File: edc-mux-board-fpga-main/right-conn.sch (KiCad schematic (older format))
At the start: 68 parts, among them J10 Device 7, J7 Device 4, J8 Device 5, J9 Device 6

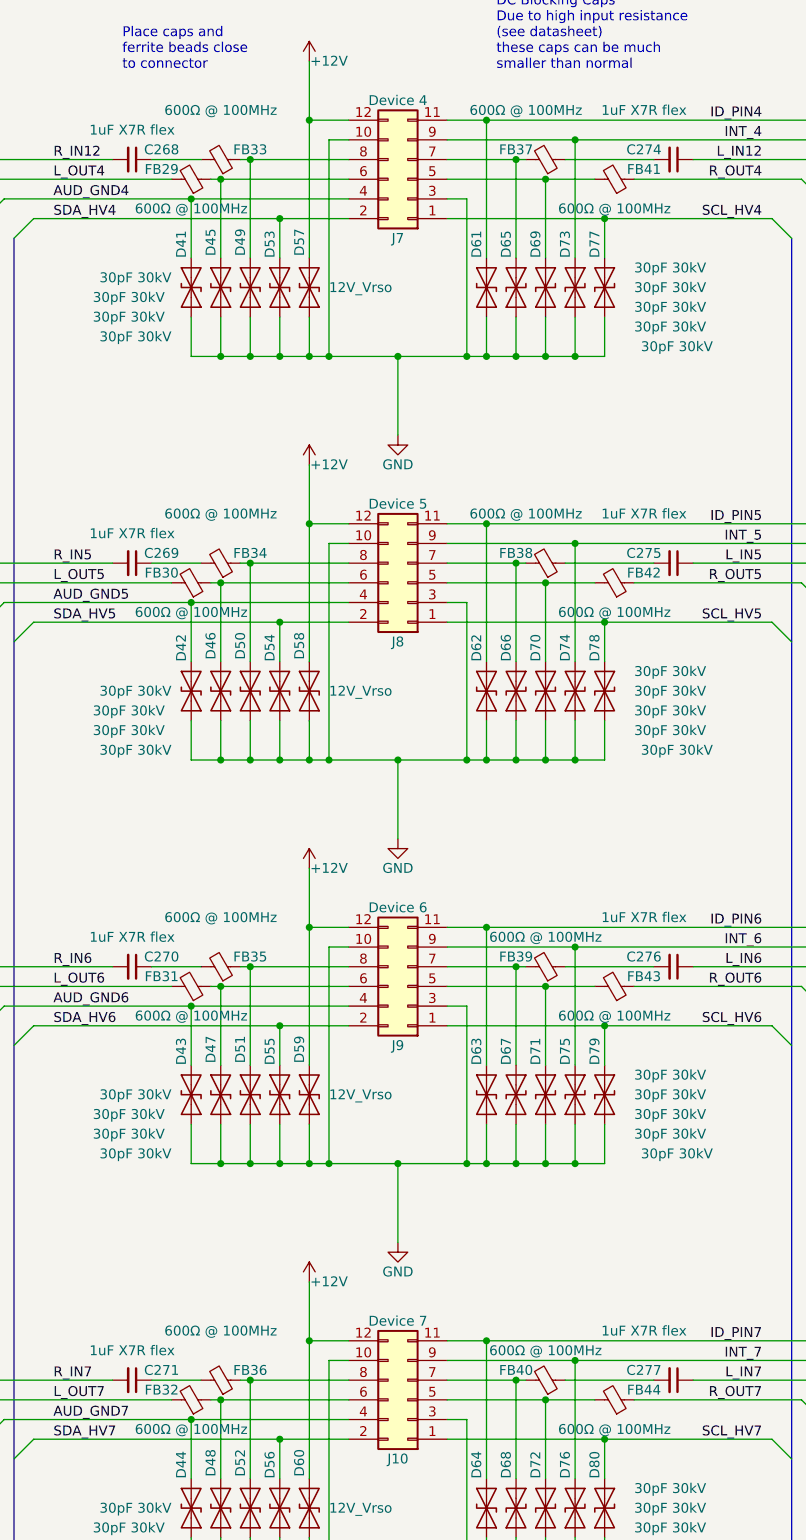
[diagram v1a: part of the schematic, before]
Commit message: Reannotate main schematic and pcb after expansion transition
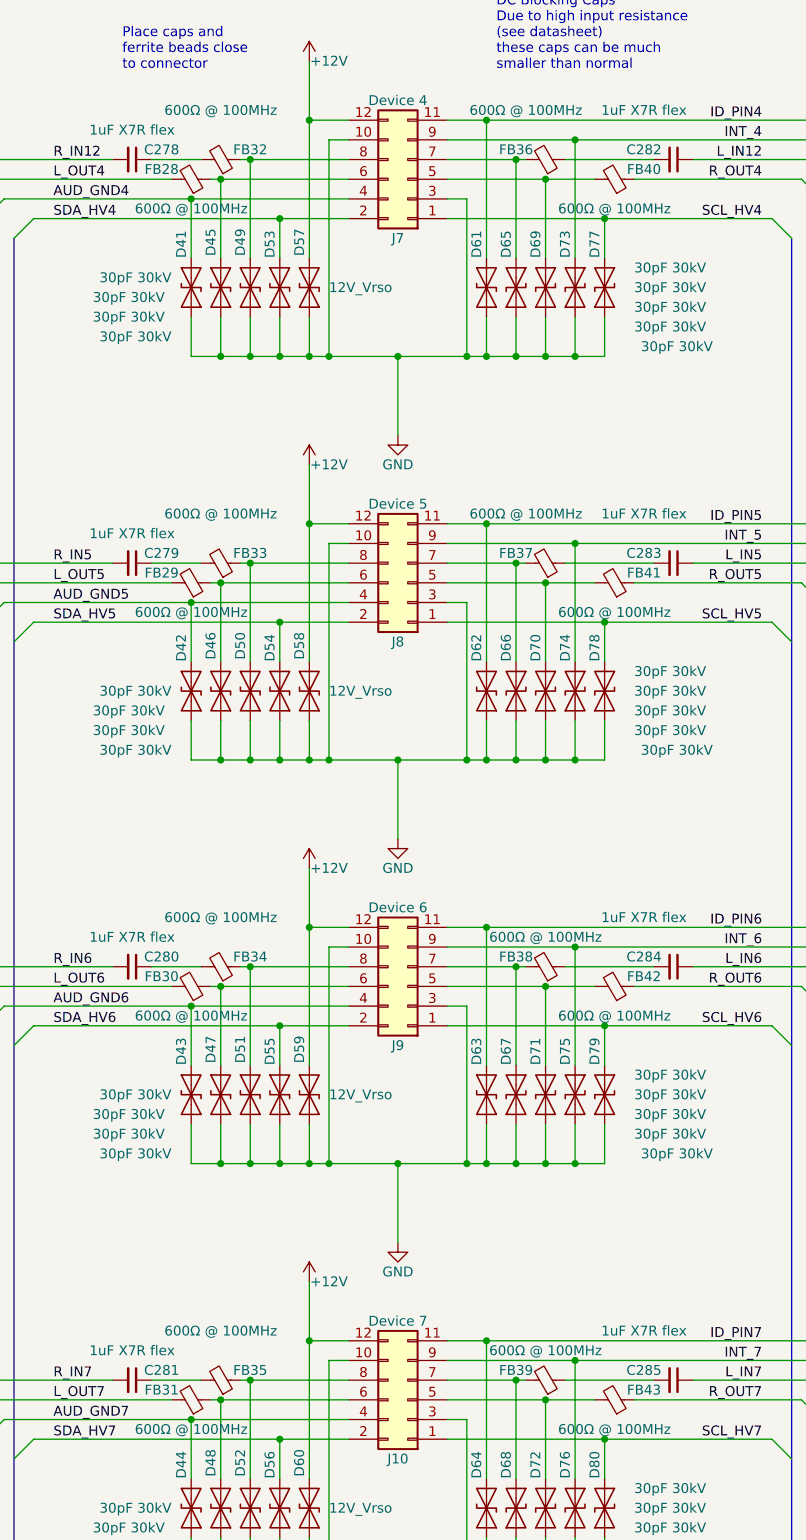
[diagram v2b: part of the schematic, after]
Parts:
- renumbered C268 to C278, C269 to C279, C270 to C280, C271 to C281, C274 to C282, C275 to C283, C276 to C284, C277 to C285, FB29 to FB28, FB30 to FB29, FB31 to FB30, FB32 to FB31, FB33 to FB32, FB34 to FB33, FB35 to FB34, FB36 to FB35, FB37 to FB36, FB38 to FB37, FB39 to FB38, FB40 to FB39, FB41 to FB40, FB42 to FB41, FB43 to FB42, FB44 to FB43
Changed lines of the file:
@@
 	4900 3100 5000 3100
 $Comp
-L power:GND #PWR0121
+L power:GND #PWR0133
 U 1 1 5D2BDD3D
 P 4550 3500
-F 0 "#PWR0121" H 4550 3250 50  0001 C CNN
+F 0 "#PWR0133" H 4550 3250 50  0001 C CNN
 F 1 "GND" H 4550 3350 50  0000 C CNN
 F 2 "" H 4550 3500 50  0001 C CNN
@@
 INT_4
 $Comp
-L power:+12V #PWR0117
+L power:+12V #PWR0129
 U 1 1 5D2BDD51
 P 4100 1600
-F 0 "#PWR0117" H 4100 1450 50  0001 C CNN
+F 0 "#PWR0129" H 4100 1450 50  0001 C CNN
 F 1 "+12V" H 4200 1600 50  0000 C CNN
 F 2 "" H 4100 1600 50  0001 C CNN
@@
 	4800 2400 5600 2400
 $Comp
-L Device:Ferrite_Bead_Small FB37
+L Device:Ferrite_Bead_Small FB36
 U 1 1 5D2BDD5F
 P 5300 2100
-F 0 "FB37" V 5350 1950 50  0000 C CNN
+F 0 "FB36" V 5350 1950 50  0000 C CNN
 F 1 "600Ω @ 100MHz" V 5550 2000 50  0000 C CNN
 F 2 "Inductor_SMD:L_0805_2012Metric" V 5230 2100 50  0001 C CNN
@@
 	3600 2200 3650 2200
 $Comp
-L Device:C_Small C268
+L Device:C_Small C278
 U 1 1 5D2BDD6B
 P 3200 2100
-F 0 "C268" V 3150 2250 50  0000 C CNN
+F 0 "C278" V 3150 2250 50  0000 C CNN
 F 1 "1uF X7R flex" V 3050 2100 50  0000 C CNN
 F 2 "Capacitor_SMD:C_0805_2012Metric" H 3200 2100 50  0001 C CNN
@@
 $EndComp
 $Comp
-L Device:Ferrite_Bead_Small FB33
+L Device:Ferrite_Bead_Small FB32
 U 1 1 5D2BDD77
 P 3650 2100
-F 0 "FB33" V 3700 2250 50  0000 C CNN
+F 0 "FB32" V 3700 2250 50  0000 C CNN
 F 1 "600Ω @ 100MHz" V 3900 2100 50  0000 C CNN
 F 2 "Inductor_SMD:L_0805_2012Metric" V 3580 2100 50  0001 C CNN
@@
 $EndComp
 $Comp
-L Device:Ferrite_Bead_Small FB29
+L Device:Ferrite_Bead_Small FB28
 U 1 1 5D2BDD82
 P 3500 2200
-F 0 "FB29" V 3550 2050 50  0000 C CNN
+F 0 "FB28" V 3550 2050 50  0000 C CNN
 F 1 "600Ω @ 100MHz" V 3350 2200 50  0000 C CNN
 F 2 "Inductor_SMD:L_0805_2012Metric" V 3430 2200 50  0001 C CNN
@@
 $EndComp
 $Comp
-L Device:Ferrite_Bead_Small FB41
+L Device:Ferrite_Bead_Small FB40
 U 1 1 5D2BDD8D
 P 5650 2200
-F 0 "FB41" V 5700 2350 50  0000 C CNN
+F 0 "FB40" V 5700 2350 50  0000 C CNN
 F 1 "600Ω @ 100MHz" V 5500 2200 50  0000 C CNN
 F 2 "Inductor_SMD:L_0805_2012Metric" V 5580 2200 50  0001 C CNN
@@
 $EndComp
 $Comp
-L Device:C_Small C274
+L Device:C_Small C282
 U 1 1 5D2BDD99
 P 5950 2100
-F 0 "C274" V 5900 1950 50  0000 C CNN
+F 0 "C282" V 5900 1950 50  0000 C CNN
 F 1 "1uF X7R flex" V 5700 1950 50  0000 C CNN
 F 2 "Capacitor_SMD:C_0805_2012Metric" H 5950 2100 50  0001 C CNN
@@
 	4900 5150 5000 5150
 $Comp
-L power:GND #PWR0122
+L power:GND #PWR0134
 U 1 1 5D2BDE54
 P 4550 5550
-F 0 "#PWR0122" H 4550 5300 50  0001 C CNN
+F 0 "#PWR0134" H 4550 5300 50  0001 C CNN
 F 1 "GND" H 4550 5400 50  0000 C CNN
 F 2 "" H 4550 5550 50  0001 C CNN
@@
 INT_5
 $Comp
-L power:+12V #PWR0118
+L power:+12V #PWR0130
 U 1 1 5D2BDE68
 P 4100 3650
-F 0 "#PWR0118" H 4100 3500 50  0001 C CNN
+F 0 "#PWR0130" H 4100 3500 50  0001 C CNN
 F 1 "+12V" H 4200 3650 50  0000 C CNN
 F 2 "" H 4100 3650 50  0001 C CNN
@@
 	4800 4450 5600 4450
 $Comp
-L Device:Ferrite_Bead_Small FB38
+L Device:Ferrite_Bead_Small FB37
 U 1 1 5D2BDE76
 P 5300 4150
-F 0 "FB38" V 5350 4000 50  0000 C CNN
+F 0 "FB37" V 5350 4000 50  0000 C CNN
 F 1 "600Ω @ 100MHz" V 5550 4050 50  0000 C CNN
 F 2 "Inductor_SMD:L_0805_2012Metric" V 5230 4150 50  0001 C CNN
@@
 	3600 4250 3650 4250
 $Comp
-L Device:C_Small C269
+L Device:C_Small C279
 U 1 1 5D2BDE82
 P 3200 4150
-F 0 "C269" V 3150 4300 50  0000 C CNN
+F 0 "C279" V 3150 4300 50  0000 C CNN
 F 1 "1uF X7R flex" V 3050 4150 50  0000 C CNN
 F 2 "Capacitor_SMD:C_0805_2012Metric" H 3200 4150 50  0001 C CNN
@@
 $EndComp
 $Comp
-L Device:Ferrite_Bead_Small FB34
+L Device:Ferrite_Bead_Small FB33
 U 1 1 5D2BDE8E
 P 3650 4150
-F 0 "FB34" V 3700 4300 50  0000 C CNN
+F 0 "FB33" V 3700 4300 50  0000 C CNN
 F 1 "600Ω @ 100MHz" V 3900 4150 50  0000 C CNN
 F 2 "Inductor_SMD:L_0805_2012Metric" V 3580 4150 50  0001 C CNN
@@
 $EndComp
 $Comp
-L Device:Ferrite_Bead_Small FB30
+L Device:Ferrite_Bead_Small FB29
 U 1 1 5D2BDE99
 P 3500 4250
-F 0 "FB30" V 3550 4100 50  0000 C CNN
+F 0 "FB29" V 3550 4100 50  0000 C CNN
 F 1 "600Ω @ 100MHz" V 3350 4250 50  0000 C CNN
 F 2 "Inductor_SMD:L_0805_2012Metric" V 3430 4250 50  0001 C CNN
@@
 $EndComp
 $Comp
-L Device:Ferrite_Bead_Small FB42
+L Device:Ferrite_Bead_Small FB41
 U 1 1 5D2BDEA4
 P 5650 4250
-F 0 "FB42" V 5700 4400 50  0000 C CNN
+F 0 "FB41" V 5700 4400 50  0000 C CNN
 F 1 "600Ω @ 100MHz" V 5500 4250 50  0000 C CNN
 F 2 "Inductor_SMD:L_0805_2012Metric" V 5580 4250 50  0001 C CNN
@@
 $EndComp
 $Comp
-L Device:C_Small C275
+L Device:C_Small C283
 U 1 1 5D2BDEB0
 P 5950 4150
-F 0 "C275" V 5900 4000 50  0000 C CNN
+F 0 "C283" V 5900 4000 50  0000 C CNN
 F 1 "1uF X7R flex" V 5700 4000 50  0000 C CNN
 F 2 "Capacitor_SMD:C_0805_2012Metric" H 5950 4150 50  0001 C CNN
@@
 	4900 7200 5000 7200
 $Comp
-L power:GND #PWR0123
+L power:GND #PWR0135
 U 1 1 5D2BDF6B
 P 4550 7600
-F 0 "#PWR0123" H 4100 7950 50  0001 C CNN
+F 0 "#PWR0135" H 4100 7950 50  0001 C CNN
 F 1 "GND" H 4550 7450 50  0000 C CNN
 F 2 "" H 4100 8200 50  0001 C CNN
@@
 INT_6
 $Comp
-L power:+12V #PWR0119
+L power:+12V #PWR0131
 U 1 1 5D2BDF7F
 P 4100 5700
-F 0 "#PWR0119" H 4100 5550 50  0001 C CNN
+F 0 "#PWR0131" H 4100 5550 50  0001 C CNN
 F 1 "+12V" H 4200 5700 50  0000 C CNN
 F 2 "" H 4100 5700 50  0001 C CNN
@@
 	4800 6500 5600 6500
 $Comp
-L Device:Ferrite_Bead_Small FB39
+L Device:Ferrite_Bead_Small FB38
 U 1 1 5D2BDF8D
 P 5300 6200
-F 0 "FB39" V 5350 6050 50  0000 C CNN
+F 0 "FB38" V 5350 6050 50  0000 C CNN
 F 1 "600Ω @ 100MHz" V 5450 6200 50  0000 C CNN
 F 2 "Inductor_SMD:L_0805_2012Metric" V 5230 6200 50  0001 C CNN
@@
 	3600 6300 3650 6300
 $Comp
-L Device:C_Small C270
+L Device:C_Small C280
 U 1 1 5D2BDF99
 P 3200 6200
-F 0 "C270" V 3150 6350 50  0000 C CNN
+F 0 "C280" V 3150 6350 50  0000 C CNN
 F 1 "1uF X7R flex" V 3050 6200 50  0000 C CNN
 F 2 "Capacitor_SMD:C_0805_2012Metric" H 3200 6200 50  0001 C CNN
@@
 $EndComp
 $Comp
-L Device:Ferrite_Bead_Small FB35
+L Device:Ferrite_Bead_Small FB34
 U 1 1 5D2BDFA5
 P 3650 6200
-F 0 "FB35" V 3700 6350 50  0000 C CNN
+F 0 "FB34" V 3700 6350 50  0000 C CNN
 F 1 "600Ω @ 100MHz" V 3900 6200 50  0000 C CNN
 F 2 "Inductor_SMD:L_0805_2012Metric" V 3580 6200 50  0001 C CNN
@@
 $EndComp
 $Comp
-L Device:Ferrite_Bead_Small FB31
+L Device:Ferrite_Bead_Small FB30
 U 1 1 5D2BDFB0
 P 3500 6300
-F 0 "FB31" V 3550 6150 50  0000 C CNN
+F 0 "FB30" V 3550 6150 50  0000 C CNN
 F 1 "600Ω @ 100MHz" V 3350 6300 50  0000 C CNN
 F 2 "Inductor_SMD:L_0805_2012Metric" V 3430 6300 50  0001 C CNN
@@
 $EndComp
 $Comp
-L Device:Ferrite_Bead_Small FB43
+L Device:Ferrite_Bead_Small FB42
 U 1 1 5D2BDFBB
 P 5650 6300
-F 0 "FB43" V 5700 6450 50  0000 C CNN
+F 0 "FB42" V 5700 6450 50  0000 C CNN
 F 1 "600Ω @ 100MHz" V 5500 6300 50  0000 C CNN
 F 2 "Inductor_SMD:L_0805_2012Metric" V 5580 6300 50  0001 C CNN
@@
 $EndComp
 $Comp
-L Device:C_Small C276
+L Device:C_Small C284
 U 1 1 5D2BDFC7
 P 5950 6200
-F 0 "C276" V 5900 6050 50  0000 C CNN
+F 0 "C284" V 5900 6050 50  0000 C CNN
 F 1 "1uF X7R flex" V 5700 6050 50  0000 C CNN
 F 2 "Capacitor_SMD:C_0805_2012Metric" H 5950 6200 50  0001 C CNN
@@
 	4900 9300 5000 9300
 $Comp
-L power:GND #PWR0124
+L power:GND #PWR0136
 U 1 1 5D2BE082
 P 4550 9700
-F 0 "#PWR0124" H 4550 9450 50  0001 C CNN
+F 0 "#PWR0136" H 4550 9450 50  0001 C CNN
 F 1 "GND" H 4550 9550 50  0000 C CNN
 F 2 "" H 4550 9700 50  0001 C CNN
@@
 INT_7
 $Comp
-L power:+12V #PWR0120
+L power:+12V #PWR0132
 U 1 1 5D2BE096
 P 4100 7800
-F 0 "#PWR0120" H 4100 7650 50  0001 C CNN
+F 0 "#PWR0132" H 4100 7650 50  0001 C CNN
 F 1 "+12V" H 4200 7800 50  0000 C CNN
 F 2 "" H 4100 7800 50  0001 C CNN
@@
 $EndComp
 $Comp
-L Device:Ferrite_Bead_Small FB40
+L Device:Ferrite_Bead_Small FB39
 U 1 1 5D2BE0A4
 P 5300 8300
-F 0 "FB40" V 5350 8150 50  0000 C CNN
+F 0 "FB39" V 5350 8150 50  0000 C CNN
 F 1 "600Ω @ 100MHz" V 5450 8300 50  0000 C CNN
 F 2 "Inductor_SMD:L_0805_2012Metric" V 5230 8300 50  0001 C CNN
@@
 	3600 8400 3650 8400
 $Comp
-L Device:C_Small C271
+L Device:C_Small C281
 U 1 1 5D2BE0B0
 P 3200 8300
-F 0 "C271" V 3150 8450 50  0000 C CNN
+F 0 "C281" V 3150 8450 50  0000 C CNN
 F 1 "1uF X7R flex" V 3050 8300 50  0000 C CNN
 F 2 "Capacitor_SMD:C_0805_2012Metric" H 3200 8300 50  0001 C CNN
@@
 $EndComp
 $Comp
-L Device:Ferrite_Bead_Small FB36
+L Device:Ferrite_Bead_Small FB35
 U 1 1 5D2BE0BC
 P 3650 8300
-F 0 "FB36" V 3700 8450 50  0000 C CNN
+F 0 "FB35" V 3700 8450 50  0000 C CNN
 F 1 "600Ω @ 100MHz" V 3900 8300 50  0000 C CNN
 F 2 "Inductor_SMD:L_0805_2012Metric" V 3580 8300 50  0001 C CNN
@@
 $EndComp
 $Comp
-L Device:Ferrite_Bead_Small FB32
+L Device:Ferrite_Bead_Small FB31
 U 1 1 5D2BE0C7
 P 3500 8400
-F 0 "FB32" V 3550 8250 50  0000 C CNN
+F 0 "FB31" V 3550 8250 50  0000 C CNN
 F 1 "600Ω @ 100MHz" V 3350 8400 50  0000 C CNN
 F 2 "Inductor_SMD:L_0805_2012Metric" V 3430 8400 50  0001 C CNN
@@
 $EndComp
 $Comp
-L Device:Ferrite_Bead_Small FB44
+L Device:Ferrite_Bead_Small FB43
 U 1 1 5D2BE0D2
 P 5650 8400
-F 0 "FB44" V 5700 8550 50  0000 C CNN
+F 0 "FB43" V 5700 8550 50  0000 C CNN
 F 1 "600Ω @ 100MHz" V 5500 8400 50  0000 C CNN
 F 2 "Inductor_SMD:L_0805_2012Metric" V 5580 8400 50  0001 C CNN
@@
 $EndComp
 $Comp
-L Device:C_Small C277
+L Device:C_Small C285
 U 1 1 5D2BE0DE
 P 5950 8300
-F 0 "C277" V 5900 8150 50  0000 C CNN
+F 0 "C285" V 5900 8150 50  0000 C CNN
 F 1 "1uF X7R flex" V 5700 8150 50  0000 C CNN
 F 2 "Capacitor_SMD:C_0805_2012Metric" H 5950 8300 50  0001 C CNN

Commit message: testing migration of device connectors and ESD diodes into conn.sch
This means that I can't have the values of the connectors be the device number but hopefully it will allow me to utilize the schematic duplication features with the connectors and diodes
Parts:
- renumbered C278 to C?, C282 to C?, C279 to C?, C283 to C?, C280 to C?, C284 to C?, C281 to C?, C285 to C?, D53 to D?, D61 to D?, D49 to D?, D45 to D?, D41 to D?, D65 to D?, D69 to D?, D73 to D?, D57 to D?, D77 to D?, D54 to D?, D62 to D?, D50 to D?, D46 to D?, D42 to D?, D66 to D?, D70 to D?, D74 to D?, D58 to D?, D78 to D?, D55 to D?, D63 to D?, D51 to D?, D47 to D?, D43 to D?, D67 to D?, D71 to D?, D75 to D?, D59 to D?, D79 to D?, D56 to D?, D64 to D?, D52 to D?, D48 to D?, D44 to D?, D68 to D?, D72 to D?, D76 to D?, D60 to D?, D80 to D?, FB36 to FB?, FB32 to FB?, FB28 to FB?, FB40 to FB?, FB37 to FB?, FB33 to FB?, FB29 to FB?, FB41 to FB?, FB38 to FB?, FB34 to FB?, FB30 to FB?, FB42 to FB?, FB39 to FB?, FB35 to FB?, FB31 to FB?, FB43 to FB?, J7 to J?, J8 to J?, J9 to J?, J10 to J?
